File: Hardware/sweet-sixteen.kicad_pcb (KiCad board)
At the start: 2 copper layers, 116 x 105 mm, 88 parts, among them P1 SDA_I, P10 VIN_O, P11 GND_O, P12 SDA_O, P13 CLK_O, P14 LE_O, P15 ~OE_O, P2 CLK_I, P3 LE_I, P4 ~OE_I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

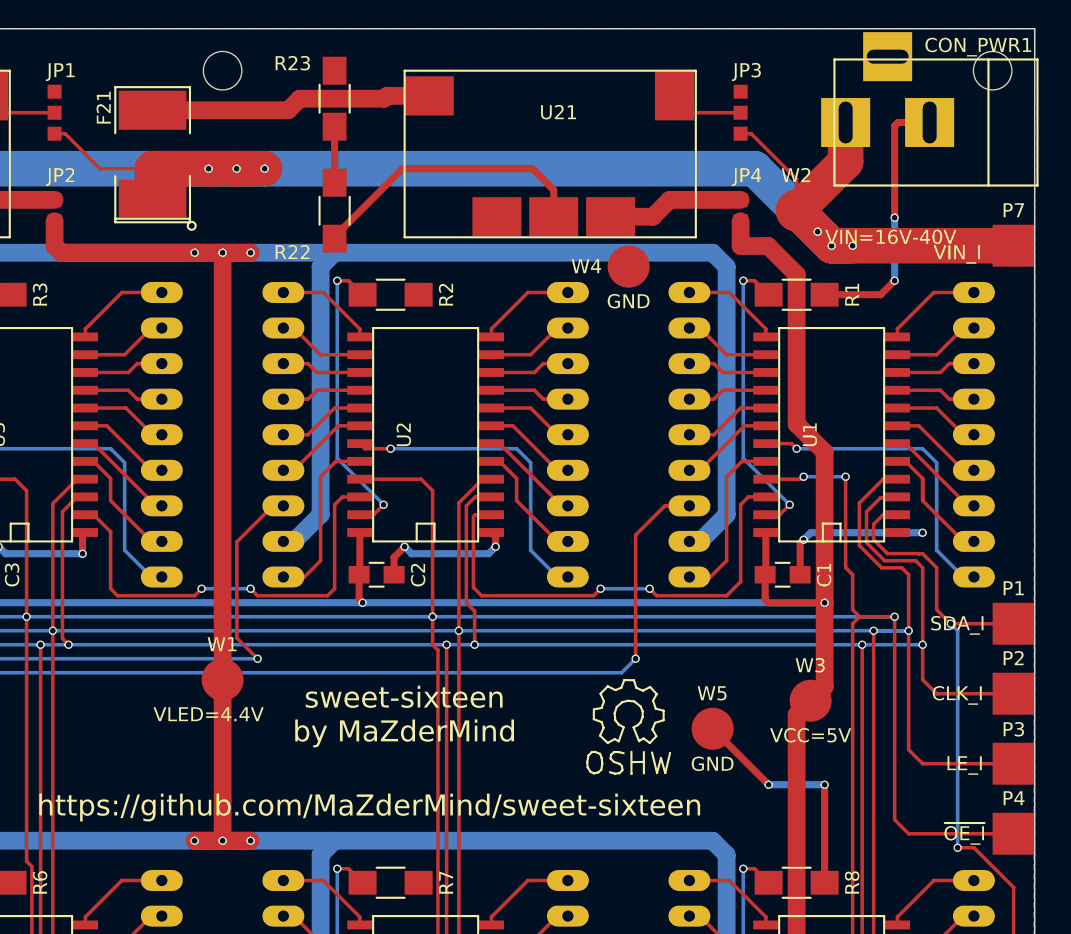
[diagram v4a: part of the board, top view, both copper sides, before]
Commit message: place new connector footprint, update gerbers with soldermask
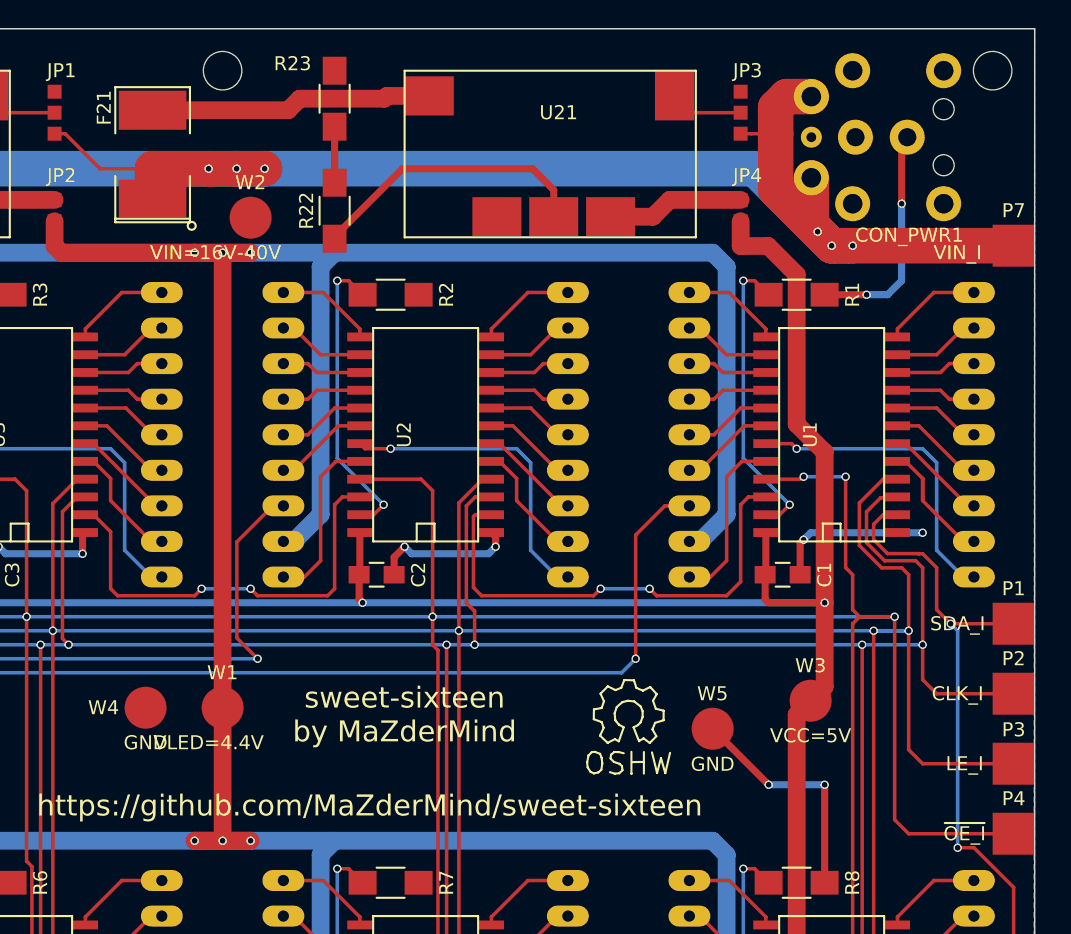
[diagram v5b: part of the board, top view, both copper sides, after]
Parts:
- CON_PWR1: footprint Connect:BARREL_JACK -> DELL-PCON:DELL-PCON
- moved W4 46.7 mm to (152.5, 98.5)
- moved W2 39.0 mm to (160.0, 63.5)
- moved CON_PWR1 2.62 mm to (206.3, 57.8)
- moved W1 2.00 mm to (158.0, 98.5)
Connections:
- CON_PWR1 pad 3: GND -> (no net)
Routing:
- net VIN: track 165.2 -> 171.6 mm
- net GND: track 233.2 -> 230.4 mm
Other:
- rule pad_to_mask_clearance: 0.254 -> 0.1524

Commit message: rev1 changes
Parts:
- removed W5: GND, Measurement_Points:Measurement_Point_Round-SMD-Pad_Big
- moved W2 57.4 mm to (103.0, 57.0)
- moved C9 2.50 mm to (149.5, 141.0)
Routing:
- net GND: track 230.4 -> 214.3 mm
- net VIN: track 171.6 -> 175.5 mm
- net VCC: track 407.9 -> 409.2 mm
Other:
- board text added: "rev2"
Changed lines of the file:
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@@
 (kicad_pcb (version 4) (host pcbnew 4.0.2+dfsg1-stable)
   (general
-    (links 330)
-    (no_connects 1)
+    (links 329)
+    (no_connects 0)
     (area 99.69481 49.281 242.796801 155.050001)
     (thickness 1.6)
-    (drawings 6)
-    (tracks 1631)
+    (drawings 7)
+    (tracks 1632)
     (zones 0)
-    (modules 88)
+    (modules 87)
     (nets 191)
   )
@@
   )
   (setup
-    (last_trace_width 0.254)
+    (last_trace_width 0.508)
     (user_trace_width 0.254)
     (user_trace_width 0.508)
@@
     (add_net VIN)
   )
+  (module Measurement_Points:Measurement_Point_Round-SMD-Pad_Big (layer F.Cu)
+    (at 152.5 98.5)
+    (descr "Mesurement Point, Round, SMD Pad, DM 3mm,")
+    (tags "Mesurement Point, Round, SMD Pad, DM 3mm,")
+    (fp_text reference W4 (at -3 0) (layer F.SilkS)
+      (effects (font (size 1 1) (thickness 0.15)))
+    )
+    (fp_text value GND (at -1.5 2.5) (layer F.SilkS)
+      (effects (font (size 1 1) (thickness 0.15)))
+    )
+    (pad 1 smd circle (at 0 0) (size 2.99974 2.99974) (layers F.Cu F.Paste F.Mask)
+      (net 139 GND))
+  )
   (module rpi-header:m25-mounting-hole (layer F.Cu)
     (at 158 53)
@@
   )
   (module Capacitors_SMD:C_0805_HandSoldering (layer F.Cu)
-    (at 147 141 90)
+    (at 149.5 141 90)
     (descr "Capacitor SMD 0805, hand soldering")
     (tags "capacitor 0805")
@@
       (effects (font (size 1 1) (thickness 0.15)) (justify mirror))
     )
-    (fp_text value LED (at 1.524 3.937 270) (layer B.Fab)
+    (fp_text value LED (at -0.6498 -4.25 360) (layer B.Fab)
       (effects (font (size 1 1) (thickness 0.15)) (justify mirror))
     )
@@
       (effects (font (size 1 1) (thickness 0.15)))
     )
-    (fp_text value VLED=4.4V (at -1 2.5) (layer F.SilkS)
+    (fp_text value VLED=4.4V (at 0 2.5) (layer F.SilkS)
       (effects (font (size 1 1) (thickness 0.15)))
     )
@@
   )
   (module Measurement_Points:Measurement_Point_Round-SMD-Pad_Big (layer F.Cu)
-    (at 160 63.5)
+    (at 103 57)
     (descr "Mesurement Point, Round, SMD Pad, DM 3mm,")
     (tags "Mesurement Point, Round, SMD Pad, DM 3mm,")
-    (fp_text reference W2 (at 0 -2.5) (layer F.SilkS)
+    (fp_text reference W2 (at -1 2.5) (layer F.SilkS)
       (effects (font (size 1 1) (thickness 0.15)))
     )
-    (fp_text value VIN=16V-40V (at -2.5 2.5) (layer F.SilkS)
+    (fp_text value VIN=16V-40V (at 6.5 1.5) (layer F.SilkS)
       (effects (font (size 1 1) (thickness 0.15)))
     )
@@
       (net 138 VCC))
   )
-  (module Measurement_Points:Measurement_Point_Round-SMD-Pad_Big (layer F.Cu)
-    (at 152.5 98.5)
-    (descr "Mesurement Point, Round, SMD Pad, DM 3mm,")
-    (tags "Mesurement Point, Round, SMD Pad, DM 3mm,")
-    (fp_text reference W4 (at -3 0) (layer F.SilkS)
-      (effects (font (size 1 1) (thickness 0.15)))
-    )
-    (fp_text value GND (at 0 2.5) (layer F.SilkS)
-      (effects (font (size 1 1) (thickness 0.15)))
-    )
-    (pad 1 smd circle (at 0 0) (size 2.99974 2.99974) (layers F.Cu F.Paste F.Mask)
-      (net 139 GND))
-  )
-  (module Measurement_Points:Measurement_Point_Round-SMD-Pad_Big (layer F.Cu)
-    (at 193 100)
-    (descr "Mesurement Point, Round, SMD Pad, DM 3mm,")
-    (tags "Mesurement Point, Round, SMD Pad, DM 3mm,")
-    (fp_text reference W5 (at 0 -2.5) (layer F.SilkS)
-      (effects (font (size 1 1) (thickness 0.15)))
-    )
-    (fp_text value GND (at 0 2.54) (layer F.SilkS)
-      (effects (font (size 1 1) (thickness 0.15)))
-    )
-    (pad 1 smd circle (at 0 0) (size 2.99974 2.99974) (layers F.Cu F.Paste F.Mask)
-      (net 139 GND))
-  )
   (module Capacitors_SMD:C_0805_HandSoldering (layer F.Cu)
     (at 186 137 270)
@@
       (effects (font (size 1 1) (thickness 0.15)))
     )
-    (fp_text value 0.1μF (at 0 2.1 270) (layer F.Fab)
+    (fp_text value 0.1μF (at 0 1.5 270) (layer F.Fab)
       (effects (font (size 1 1) (thickness 0.15)))
     )
@@
       (effects (font (size 1 1) (thickness 0.15)))
     )
-    (fp_text value 0.1μF (at 0 2.1 270) (layer F.Fab)
+    (fp_text value 0.1μF (at 0 -1.5 270) (layer F.Fab)
       (effects (font (size 1 1) (thickness 0.15)))
     )
@@
       (effects (font (size 1 1) (thickness 0.15)))
     )
-    (fp_text value "1.2A F" (at 0 0 180) (layer F.Fab)
+    (fp_text value "1.2A F" (at 5.5 0 180) (layer F.Fab)
       (effects (font (size 1 1) (thickness 0.15)))
     )
@@
     (pad "" np_thru_hole circle (at -3.2 2 180) (size 1.5 1.5) (drill 1.5) (layers *.Cu *.Mask F.SilkS))
   )
+  (gr_text rev2 (at 102 151.5 90) (layer F.Cu)
+    (effects (font (size 1.5 1.5) (thickness 0.3)))
+  )
   (gr_text https://github.com/MaZderMind/sweet-sixteen (at 168.5 105.5) (layer F.SilkS)
     (effects (font (size 1.5 1.5) (thickness 0.3)))
@@
   (segment (start 211.66 131.16) (end 210.91 131.16) (width 0.254) (layer B.Cu) (net 137) (status 30))
   (segment (start 210.91 131.16) (end 209 129.25) (width 0.254) (layer B.Cu) (net 137) (status 10))
+  (segment (start 138.75 131) (end 138.75 132.5) (width 0.508) (layer F.Cu) (net 138))
+  (segment (start 138.75 132.5) (end 139.058999 132.808999) (width 0.508) (layer F.Cu) (net 138))
+  (segment (start 139.058999 132.808999) (end 149.308999 132.808999) (width 0.508) (layer F.Cu) (net 138))
+  (segment (start 149.308999 132.808999) (end 150 133.5) (width 0.508) (layer F.Cu) (net 138))
+  (segment (start 166.596 133.5) (end 150 133.5) (width 0.508) (layer F.Cu) (net 138))
+  (segment (start 150.633001 134.133001) (end 150 133.5) (width 0.508) (layer F.Cu) (net 138))
+  (segment (start 149.5 142.25) (end 149.5 142.125) (width 0.508) (layer F.Cu) (net 138))
+  (segment (start 149.5 142.125) (end 150.633001 140.991999) (width 0.508) (layer F.Cu) (net 138))
+  (segment (start 150.633001 140.991999) (end 150.633001 134.133001) (width 0.508) (layer F.Cu) (net 138))
+  (segment (start 147 142.25) (end 149.5 142.25) (width 0.508) (layer F.Cu) (net 138))
   (segment (start 195 65.52) (end 196.970202 65.52) (width 1.27) (layer F.Cu) (net 138))
   (segment (start 195 63.75) (end 195 65.52) (width 1.27) (layer F.Cu) (net 138) (status 10))
@@
   (segment (start 145.867 142.25) (end 145.985 142.368) (width 0.508) (layer F.Cu) (net 138))
   (segment (start 145.985 142.368) (end 145.985 145.699) (width 0.508) (layer F.Cu) (net 138) (status 20))
-  (segment (start 149 141.383) (end 149 133.5) (width 0.508) (layer F.Cu) (net 138))
-  (segment (start 149 133.5) (end 149 132.808999) (width 0.508) (layer F.Cu) (net 138))
-  (segment (start 166.596 133.5) (end 149 133.5) (width 0.508) (layer F.Cu) (net 138))
   (segment (start 167.175 137) (end 167.175 134.079) (width 0.508) (layer F.Cu) (net 138) (status 10))
   (segment (start 167.175 134.079) (end 166.596 133.5) (width 0.508) (layer F.Cu) (net 138))
@@
   (segment (start 147 142.25) (end 145.867 142.25) (width 0.508) (layer F.Cu) (net 138) (status 10))
   (segment (start 145.867 142.25) (end 144.617 141) (width 0.508) (layer F.Cu) (net 138))
-  (segment (start 138.75 131) (end 138.75 132.5) (width 0.508) (layer F.Cu) (net 138) (status 10))
-  (segment (start 149 132.808999) (end 139.058999 132.808999) (width 0.508) (layer F.Cu) (net 138))
-  (segment (start 139.058999 132.808999) (end 138.75 132.5) (width 0.508) (layer F.Cu) (net 138))
   (segment (start 199 67.549798) (end 199 78.24199) (width 1.27) (layer F.Cu) (net 138))
   (segment (start 199 78.24199) (end 201 80.24199) (width 1.27) (layer F.Cu) (net 138))
@@
   (segment (start 105.42887 134.07113) (end 106.691001 132.808999) (width 0.508) (layer F.Cu) (net 138))
   (segment (start 105.42887 134.079) (end 105.42887 134.07113) (width 0.508) (layer F.Cu) (net 138))
-  (segment (start 147 142.25) (end 148.133 142.25) (width 0.508) (layer F.Cu) (net 138) (status 10))
-  (segment (start 148.133 142.25) (end 149 141.383) (width 0.508) (layer F.Cu) (net 138))
   (segment (start 196.75 90.75) (end 197 91) (width 0.508) (layer F.Cu) (net 138))
   (segment (start 197 91) (end 201 91) (width 0.508) (layer F.Cu) (net 138))
@@
   (segment (start 199 99) (end 199 120) (width 1.27) (layer F.Cu) (net 138) (status 10))
   (segment (start 199 120) (end 201 122) (width 1.27) (layer F.Cu) (net 138))
+  (segment (start 201 104) (end 197 104) (width 0.508) (layer B.Cu) (net 139))
   (segment (start 206.5 62.5) (end 206.5 58.15) (width 0.508) (layer F.Cu) (net 139))
   (segment (start 206.5 58.15) (end 206.9 57.75) (width 0.508) (layer F.Cu) (net 139))
@@
   (segment (start 201 69) (end 204 69) (width 0.508) (layer F.Cu) (net 139))
   (via (at 204 69) (size 0.6) (drill 0.4) (layers F.Cu B.Cu) (net 139))
-  (segment (start 197 104) (end 193 100) (width 0.508) (layer F.Cu) (net 139) (status 20))
-  (segment (start 201 104) (end 197 104) (width 0.508) (layer B.Cu) (net 139))
   (via (at 197 104) (size 0.6) (drill 0.4) (layers F.Cu B.Cu) (net 139))
   (segment (start 201 111) (end 201 104) (width 0.508) (layer F.Cu) (net 139) (status 10))
@@
   (segment (start 114 111) (end 114.15 111) (width 0.508) (layer F.Cu) (net 139) (status 30))
   (segment (start 114.15 111) (end 118.65 106.5) (width 0.508) (layer F.Cu) (net 139) (status 10))
-  (segment (start 109.5 101.5) (end 110.5 100.5) (width 0.508) (layer B.Cu) (net 139))
-  (segment (start 110.5 100.5) (end 119.5 100.5) (width 0.508) (layer B.Cu) (net 139))
   (segment (start 114.5 89) (end 112.25 89) (width 0.508) (layer F.Cu) (net 139) (status 20))
   (segment (start 115 88.5) (end 114.5 89) (width 0.508) (layer B.Cu) (net 139))
@@
   (segment (start 140.905 146.332302) (end 141.867467 147.294769) (width 0.254) (layer F.Cu) (net 147) (status 10))
   (segment (start 140.905 145.699) (end 140.905 146.1435) (width 0.254) (layer F.Cu) (net 147) (status 30))
+  (segment (start 105 60) (end 105 59) (width 0.254) (layer F.Cu) (net 148))
+  (segment (start 105 59) (end 103 57) (width 0.254) (layer F.Cu) (net 148))
   (segment (start 197.5 55.632234) (end 197.5 57.5) (width 2.54) (layer F.Cu) (net 148))
   (segment (start 197.5 57.5) (end 197.5 61.5) (width 2.54) (layer F.Cu) (net 148))
